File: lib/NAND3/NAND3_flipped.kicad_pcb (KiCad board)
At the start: 2 copper layers, 6 parts

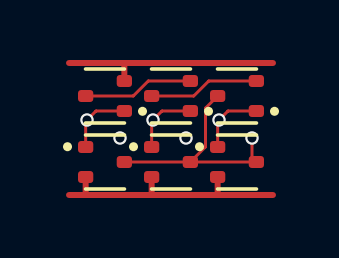
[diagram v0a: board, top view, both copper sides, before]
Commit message: All cells now use 1mm*4mm grid rather than 1.1mm*4.4mm
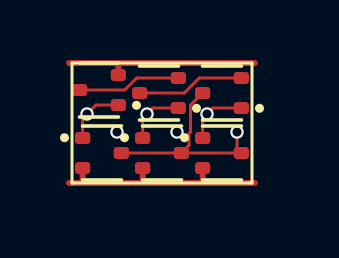
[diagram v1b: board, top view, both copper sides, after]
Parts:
- moved P3 0.58 mm to (5.00, 3.00)
- moved N3 0.51 mm to (5.00, 1.00)
- moved P2 0.42 mm to (3.00, 3.00)
- moved N2 0.41 mm to (2.90, 1.00)
- moved P1 0.32 mm to (1.00, 3.00)
- moved N1 0.28 mm to (0.90, 0.90)
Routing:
- net Y: track 7.99 -> 6.85 mm
- net VDD: track 8.63 -> 7.65 mm
- net GND: track 7.42 -> 6.62 mm
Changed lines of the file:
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@@
 	(footprint "Package_TO_SOT_SMD:SOT-523"
 		(layer "F.Cu")
-		(at 5.5 3.3)
+		(at 5 3)
 		(descr "SOT523, https://www.diodes.com/assets/Package-Files/SOT523.pdf")
 		(tags "SOT-523")
@@
 	(footprint "Package_TO_SOT_SMD:SOT-523"
 		(layer "F.Cu")
-		(at 1.1 3.3)
+		(at 1 3)
 		(descr "SOT523, https://www.diodes.com/assets/Package-Files/SOT523.pdf")
 		(tags "SOT-523")
@@
 	(footprint "Package_TO_SOT_SMD:SOT-523"
 		(layer "F.Cu")
-		(at 5.5 1.1 180)
+		(at 5 1 180)
 		(descr "SOT523, https://www.diodes.com/assets/Package-Files/SOT523.pdf")
 		(tags "SOT-523")
@@
 	(footprint "Package_TO_SOT_SMD:SOT-523"
 		(layer "F.Cu")
-		(at 3.3 3.3)
+		(at 3 3)
 		(descr "SOT523, https://www.diodes.com/assets/Package-Files/SOT523.pdf")
 		(tags "SOT-523")
@@
 	(footprint "Package_TO_SOT_SMD:SOT-523"
 		(layer "F.Cu")
-		(at 3.3 1.1 180)
+		(at 2.9 1 180)
 		(descr "SOT523, https://www.diodes.com/assets/Package-Files/SOT523.pdf")
 		(tags "SOT-523")
@@
 	(footprint "Package_TO_SOT_SMD:SOT-523"
 		(layer "F.Cu")
-		(at 1.1 1.1 180)
+		(at 0.9 0.9 180)
 		(descr "SOT523, https://www.diodes.com/assets/Package-Files/SOT523.pdf")
 		(tags "SOT-523")
@@
 		)
 	)
+	(gr_rect
+		(start 0 0)
+		(end 6 4)
+		(stroke
+			(width 0.1)
+			(type default)
+		)
+		(fill no)
+		(layer "F.SilkS")
+	)
 	(via
-		(at 3.8 2.5)
+		(at 3.5 2.3)
 		(size 0.45)
 		(drill 0.3)
@@
 	)
 	(via
-		(at 1.6 2.5)
+		(at 1.5 2.3)
 		(size 0.45)
 		(drill 0.3)
@@
 	)
 	(segment
-		(start 1.745 0.045)
+		(start -0.1 0)
+		(end 1.6 0)
+		(width 0.2)
+		(layer "F.Cu")
+		(net 1)
+	)
+	(segment
+		(start 1.6 0)
 		(end 1.7 0)
 		(width 0.2)
@@
 	)
 	(segment
-		(start -0.1 0)
-		(end 1.7 0)
+		(start 1.545 0.4)
+		(end 1.545 0.055)
 		(width 0.2)
 		(layer "F.Cu")
@@
 	)
 	(segment
-		(start 1.745 0.6)
-		(end 1.745 0.045)
+		(start 1.7 0)
+		(end 6.1 0)
 		(width 0.2)
 		(layer "F.Cu")
@@
 	)
 	(segment
-		(start 1.7 0)
-		(end 6.7 0)
+		(start 1.545 0.055)
+		(end 1.6 0)
 		(width 0.2)
 		(layer "F.Cu")
@@
 	)
 	(segment
-		(start 4.45 1.505)
-		(end 4.45 2.795)
+		(start 1.645 3)
+		(end 3.645 3)
 		(width 0.1)
 		(layer "F.Cu")
@@
 	)
 	(segment
-		(start 4.45 2.795)
-		(end 3.945 3.3)
+		(start 3.9 2.342262)
+		(end 3.9 2.745)
 		(width 0.1)
 		(layer "F.Cu")
@@
 	)
 	(segment
-		(start 1.745 3.3)
-		(end 3.945 3.3)
+		(start 5.5 2.3)
+		(end 5.5 2.855)
 		(width 0.1)
 		(layer "F.Cu")
@@
 	)
 	(segment
-		(start 6.25 3.195)
-		(end 6.145 3.3)
+		(start 3.951 2.291262)
+		(end 3.9 2.342262)
 		(width 0.1)
 		(layer "F.Cu")
@@
 	)
 	(segment
-		(start 3.945 3.3)
-		(end 6.145 3.3)
+		(start 4.355 1)
+		(end 3.951 1.404)
 		(width 0.1)
 		(layer "F.Cu")
@@
 	)
 	(segment
-		(start 4.855 1.1)
-		(end 4.45 1.505)
+		(start 3.645 3)
+		(end 5.645 3)
 		(width 0.1)
 		(layer "F.Cu")
@@
 	)
 	(segment
-		(start 6 3.155)
-		(end 6.145 3.3)
+		(start 3.951 1.404)
+		(end 3.951 2.291262)
 		(width 0.1)
 		(layer "F.Cu")
@@
 	)
 	(segment
-		(start 6 2.5)
-		(end 6 3.155)
+		(start 3.9 2.745)
+		(end 3.645 3)
 		(width 0.1)
 		(layer "F.Cu")
@@
 	)
 	(via
-		(at 6 2.5)
+		(at 5.5 2.3)
 		(size 0.45)
 		(drill 0.3)
@@
 	)
 	(segment
-		(start 6.145 1.6)
-		(end 5.2 1.6)
+		(start 4.355 1.845)
+		(end 4.5 1.7)
 		(width 0.1)
 		(layer "F.Cu")
@@
 	)
 	(segment
-		(start 4.855 1.945)
-		(end 4.9 1.9)
+		(start 4.5 1.7)
+		(end 4.7 1.5)
 		(width 0.1)
 		(layer "F.Cu")
@@
 	)
 	(segment
-		(start 5.2 1.6)
-		(end 4.9 1.9)
+		(start 4.7 1.5)
+		(end 5.645 1.5)
 		(width 0.1)
 		(layer "F.Cu")
@@
 	)
 	(segment
-		(start 4.855 2.8)
-		(end 4.855 1.945)
+		(start 4.355 2.5)
+		(end 4.355 1.845)
 		(width 0.1)
 		(layer "F.Cu")
@@
 	)
 	(via
-		(at 4.9 1.9)
+		(at 4.5 1.7)
 		(size 0.45)
 		(drill 0.3)
@@
 	)
 	(segment
-		(start 2.655 4.395)
-		(end 2.65 4.4)
+		(start 2.355 3.5)
+		(end 2.355 3.945)
 		(width 0.2)
 		(layer "F.Cu")
@@
 	)
 	(segment
-		(start 0.455 4.395)
-		(end 0.45 4.4)
+		(start 2.355 3.945)
+		(end 2.3 4)
 		(width 0.2)
 		(layer "F.Cu")
@@
 	)
 	(segment
-		(start 0.455 3.8)
-		(end 0.455 4.395)
+		(start 4.355 3.5)
+		(end 4.355 3.955)
 		(width 0.2)
 		(layer "F.Cu")
@@
 	)
 	(segment
-		(start 2.655 3.8)
-		(end 2.655 4.395)
+		(start 4.355 3.955)
+		(end 4.4 4)
 		(width 0.2)
 		(layer "F.Cu")
@@
 	)
 	(segment
-		(start 4.855 4.345)
-		(end 4.8 4.4)
+		(start 2.3 4)
+		(end 2.65 4)
 		(width 0.2)
 		(layer "F.Cu")
@@
 	)
 	(segment
-		(start 4.855 3.8)
-		(end 4.855 4.345)
+		(start 2.65 4)
+		(end 4.4 4)
 		(width 0.2)
 		(layer "F.Cu")
@@
 	)
 	(segment
-		(start 2.65 4.4)
-		(end 4.8 4.4)
+		(start -0.1 4)
+		(end 0.45 4)
 		(width 0.2)
 		(layer "F.Cu")
@@
 	)
 	(segment
-		(start -0.1 4.4)
-		(end 0.45 4.4)
+		(start 4.4 4)
+		(end 4.8 4)
 		(width 0.2)
 		(layer "F.Cu")
@@
 	)
 	(segment
-		(start 0.45 4.4)
-		(end 2.65 4.4)
+		(start 0.45 4)
+		(end 2.3 4)
 		(width 0.2)
 		(layer "F.Cu")
@@
 	)
 	(segment
-		(start 4.8 4.4)
-		(end 6.7 4.4)
+		(start 4.8 4)
+		(end 6.1 4)
 		(width 0.2)
 		(layer "F.Cu")
@@
 	)
 	(segment
-		(start 0.455 2.8)
-		(end 0.455 1.945)
+		(start 0.355 3.5)
+		(end 0.355 3.905)
+		(width 0.2)
+		(layer "F.Cu")
+		(net 4)
+	)
+	(segment
+		(start 0.355 1.845)
+		(end 0.5 1.7)
 		(width 0.1)
 		(layer "F.Cu")
@@
 	)
 	(segment
-		(start 0.455 1.945)
-		(end 0.5 1.9)
+		(start 0.8 1.4)
+		(end 1.545 1.4)
 		(width 0.1)
 		(layer "F.Cu")
@@
 	)
 	(segment
-		(start 0.8 1.6)
-		(end 0.5 1.9)
+		(start 0.355 2.5)
+		(end 0.355 1.845)
 		(width 0.1)
 		(layer "F.Cu")
@@
 	)
 	(segment
-		(start 1.745 1.6)
-		(end 0.8 1.6)
+		(start 0.5 1.7)
+		(end 0.8 1.4)
 		(width 0.1)
 		(layer "F.Cu")
@@
 	)
 	(via
-		(at 0.5 1.9)
+		(at 0.5 1.7)
 		(size 0.45)
 		(drill 0.3)
@@
 	)
 	(segment
-		(start 3.945 1.6)
-		(end 3 1.6)
+		(start 2.5 1.7)
+		(end 2.7 1.5)
 		(width 0.1)
 		(layer "F.Cu")
@@
 	)
 	(segment
-		(start 3 1.6)
-		(end 2.7 1.9)
+		(start 2.355 1.845)
+		(end 2.5 1.7)
 		(width 0.1)
 		(layer "F.Cu")
@@
 	)
 	(segment
-		(start 2.655 2.8)
-		(end 2.655 1.945)
+		(start 2.355 2.5)
+		(end 2.355 1.845)
 		(width 0.1)
 		(layer "F.Cu")
@@
 	)
 	(segment
-		(start 2.655 1.945)
-		(end 2.7 1.9)
+		(start 2.7 1.5)
+		(end 3.545 1.5)
 		(width 0.1)
 		(layer "F.Cu")
@@
 	)
 	(via
-		(at 2.7 1.9)
+		(at 2.5 1.7)
 		(size 0.45)
 		(drill 0.3)
@@
 	)
 	(segment
-		(start 2.542262 0.6)
-		(end 2.042262 1.1)
+		(start 1.757738 0.9)
+		(end 2.157738 0.5)
 		(width 0.1)
 		(layer "F.Cu")
@@
 	)
 	(segment
-		(start 3.945 0.6)
-		(end 2.542262 0.6)
+		(start 2.157738 0.5)
+		(end 3.645 0.5)
 		(width 0.1)
 		(layer "F.Cu")
@@
 	)
 	(segment
-		(start 2.042262 1.1)
-		(end 0.455 1.1)
+		(start 0.355 0.9)
+		(end 1.757738 0.9)
 		(width 0.1)
 		(layer "F.Cu")
@@
 	)
 	(segment
-		(start 4.557738 0.6)
-		(end 4.057738 1.1)
+		(start 4.242262 0.5)
+		(end 5.645 0.5)
 		(width 0.1)
 		(layer "F.Cu")
@@
 	)
 	(segment
-		(start 6.145 0.6)
-		(end 4.557738 0.6)
+		(start 2.255 1)
+		(end 3.742262 1)
 		(width 0.1)
 		(layer "F.Cu")
@@
 	)
 	(segment
-		(start 4.057738 1.1)
-		(end 2.655 1.1)
-		(width 0.1)
-		(layer "F.Cu")
+		(start 3.742262 1)
+		(end 4.242262 0.5)
+		(width 0.1)
+		(layer "F.Cu")

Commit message: Make the pads of my SOT523 footprint very slightly smaller, which is enough to route all the cells and leave the mosfets exactly on the grid
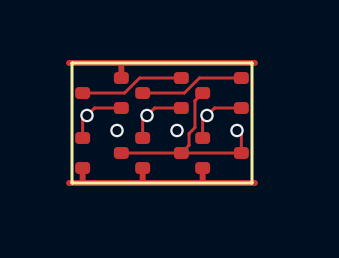
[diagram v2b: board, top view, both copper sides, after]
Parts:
- N1, N2, N3, P1, P2, P3: footprint Package_TO_SOT_SMD:SOT-523 -> RV523:SOT523
- moved N1 0.14 mm to (1.00, 1.00)
- moved N2 0.10 mm to (3.00, 1.00)

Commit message: Propagate MOSFET values to the cells' PCBs
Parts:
- N1, N2, N3: value (none) -> NMOS
- P1, P2, P3: value (none) -> PMOS
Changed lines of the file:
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@@
 			)
 		)
-		(property "Value" ""
+		(property "Value" "PMOS"
 			(at 0 0 0)
 			(layer "F.Fab")
@@
 			)
 		)
-		(property "Value" ""
+		(property "Value" "PMOS"
 			(at 0 0 0)
 			(layer "F.Fab")
@@
 			)
 		)
-		(property "Value" ""
+		(property "Value" "NMOS"
 			(at 0 0 180)
 			(layer "F.Fab")
@@
 			)
 		)
-		(property "Value" ""
+		(property "Value" "PMOS"
 			(at 0 0 0)
 			(layer "F.Fab")
@@
 			)
 		)
-		(property "Value" ""
+		(property "Value" "NMOS"
 			(at 0 0 180)
 			(layer "F.Fab")
@@
 			)
 		)
-		(property "Value" ""
-			(at 0 0 180)
-			(layer "F.Fab")
+		(property "Value" "NMOS"
+			(at 0 0 180)
+			(layer "F.Fab")
